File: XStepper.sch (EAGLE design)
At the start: 74 parts, among them Q2 16 MHZ

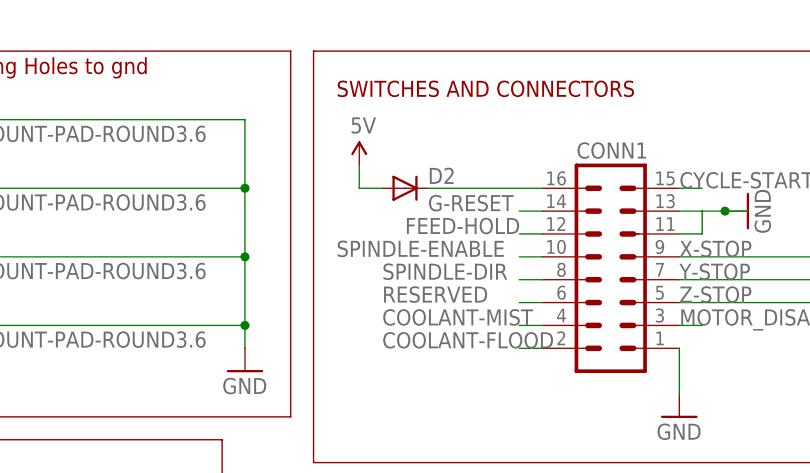
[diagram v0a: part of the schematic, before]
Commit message: Revert "- bugfix diode"
This reverts commit 7209bcb696f77dd3d5512bdf8e28195d083f39f3.
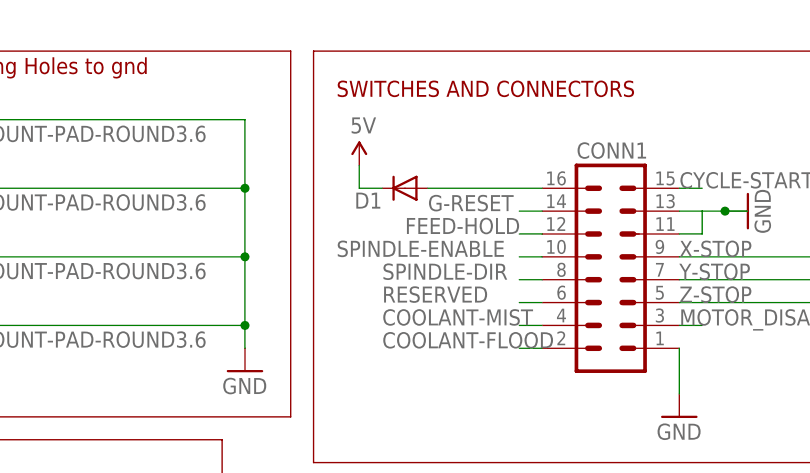
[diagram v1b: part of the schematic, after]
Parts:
- renumbered D2 to D1
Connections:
- net 5V: now also D1.C; no longer D1.A
- net N$45: now also D1.A; no longer D1.C
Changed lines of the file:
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@@
 </variantdefs>
 <classes>
-<class number="0" name="default" width="0.3048" drill="0">
-<clearance class="0" value="0.2032"/>
+<class number="0" name="default" width="0.4064" drill="0">
+<clearance class="0" value="0.254"/>
 </class>
 <class number="1" name="power" width="1.016" drill="0">
@@
 <part name="R13" library="SparkFun-Resistors" deviceset="RESISTOR" device="AXIAL-0.3"/>
 <part name="R14" library="SparkFun-Resistors" deviceset="RESISTOR" device="AXIAL-0.3"/>
+<part name="D1" library="SparkFun-DiscreteSemi" deviceset="DIODE" device="PTH"/>
 <part name="&lt;ESTOP" library="con-ptr500" deviceset="AK500/2" device=""/>
 <part name="GND39" library="SparkFun" deviceset="GND" device=""/>
@@
 <part name="GND" library="jumper" deviceset="JP1E" device=""/>
 <part name="GND21" library="SparkFun" deviceset="GND" device=""/>
-<part name="D2" library="SparkFun-DiscreteSemi" deviceset="DIODE" device="PTH"/>
 </parts>
 <sheets>
@@
 <instance part="R13" gate="G$1" x="332.74" y="165.1" rot="R270"/>
 <instance part="R14" gate="G$1" x="340.36" y="165.1" rot="R270"/>
+<instance part="D1" gate="G$1" x="236.22" y="165.1" rot="R180"/>
 <instance part="&lt;ESTOP" gate="-1" x="15.24" y="0"/>
 <instance part="&lt;ESTOP" gate="-2" x="15.24" y="-7.62"/>
@@
 <instance part="GND" gate="A" x="22.86" y="121.92" rot="R90"/>
 <instance part="GND21" gate="1" x="30.48" y="124.46" rot="R90"/>
-<instance part="D2" gate="G$1" x="236.22" y="165.1"/>
 </instances>
 <busses>
@@
 </segment>
 <segment>
+<pinref part="D1" gate="G$1" pin="C"/>
 <pinref part="U$16" gate="G$1" pin="5V"/>
 <wire x1="233.68" y1="165.1" x2="231.14" y2="165.1" width="0.1524" layer="91"/>
 <wire x1="231.14" y1="165.1" x2="231.14" y2="167.64" width="0.1524" layer="91"/>
-<pinref part="D2" gate="G$1" pin="A"/>
 </segment>
 </net>
@@
 </segment>
 </net>
-<net name="PWRMOT" class="1">
+<net name="PWRMOT" class="0">
 <segment>
 <pinref part="MOT" gate="-1" pin="KL"/>
@@
 <segment>
 <pinref part="CONN1" gate="1" pin="16"/>
+<pinref part="D1" gate="G$1" pin="A"/>
 <wire x1="251.46" y1="165.1" x2="238.76" y2="165.1" width="0.1524" layer="91"/>
-<pinref part="D2" gate="G$1" pin="C"/>
-</segment>
-</net>
+</segment>
+</net>
